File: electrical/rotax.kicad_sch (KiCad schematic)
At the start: 14 parts

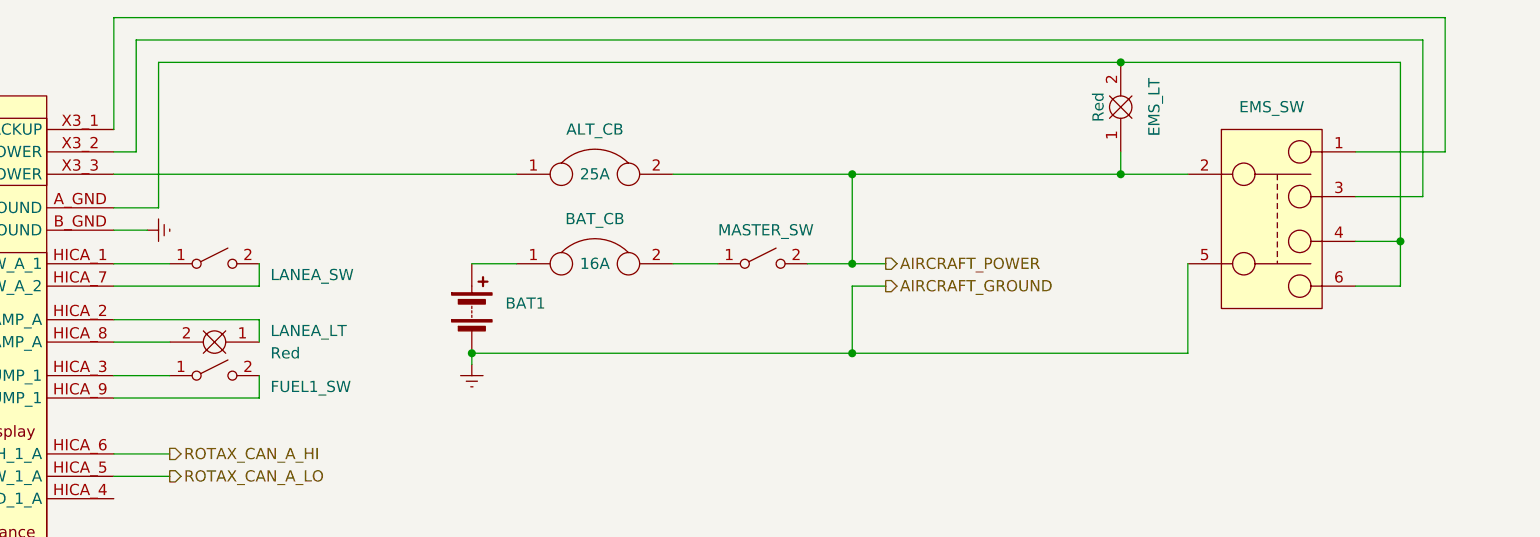
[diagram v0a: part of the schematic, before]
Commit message: Converted to breakers w/GAD 27 instead of VP-X.
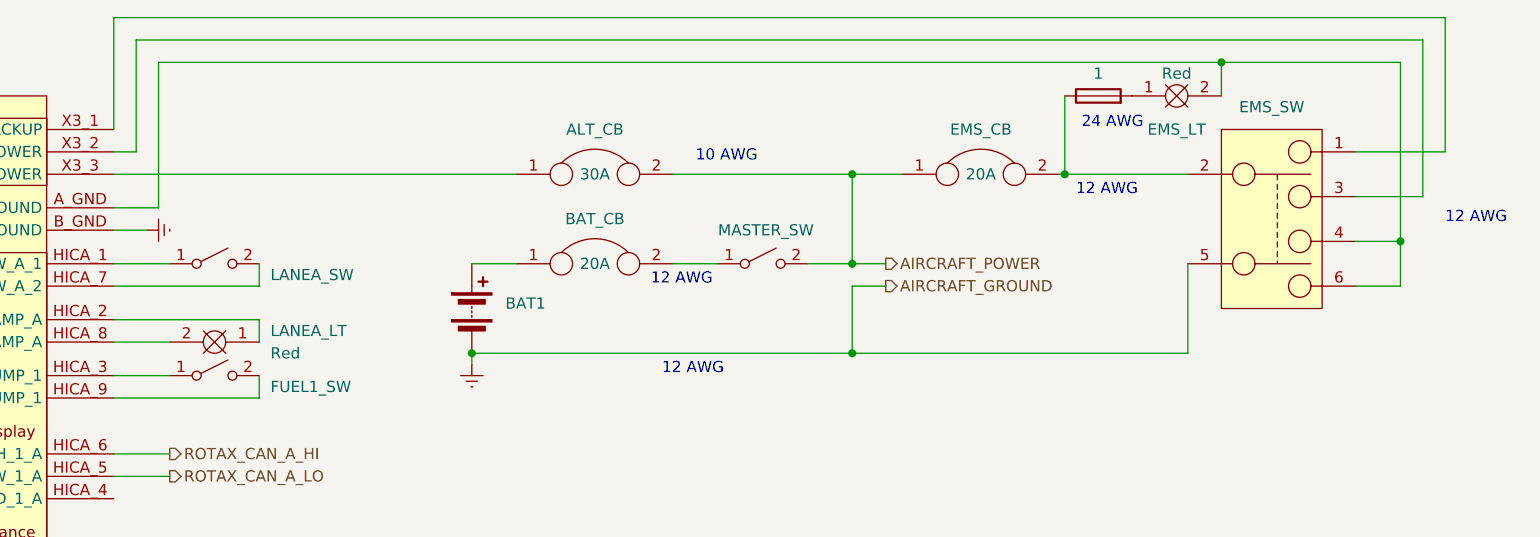
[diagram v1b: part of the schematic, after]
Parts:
- added EMS_CB: 20A, symbol flyerx:Circuit_Breaker
- added EMS_LT_FS: 1, symbol Device:Fuse
- ALT_CB: value 25A -> 30A
- BAT_CB: value 16A -> 20A
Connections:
- net AIRCRAFT_POWER: now also EMS_CB.1; no longer EMS_LT.1, EMS_SW.2
- new net: EMS_LT.1, EMS_LT_FS.2
- new net: EMS_CB.2, EMS_LT_FS.1, EMS_SW.2
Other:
- note added: "10 AWG"
- note added: "12 AWG"
- note added: "24 AWG"
- moved on the sheet: EMS_LT
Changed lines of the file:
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@@
     (title "Rotax Engine")
     (date "2024-02-13")
-    (rev "0.9.1")
+    (rev "1.0")
     (company "N915SN Angry Bird")
-  )
-  (junction (at 201.93 69.85) (diameter 0) (color 0 0 0 0)
+    (comment 1 "w/Breakers")
   )
   (junction (at 233.68 77.47) (diameter 0) (color 0 0 0 0)
   )
+  (junction (at 213.36 57.15) (diameter 0) (color 0 0 0 0)
+  )
   (junction (at 128.27 90.17) (diameter 0) (color 0 0 0 0)
   )
+  (junction (at 195.58 69.85) (diameter 0) (color 0 0 0 0)
+  )
   (junction (at 171.45 90.17) (diameter 0) (color 0 0 0 0)
   )
@@
   (junction (at 171.45 80.01) (diameter 0) (color 0 0 0 0)
   )
-  (junction (at 201.93 57.15) (diameter 0) (color 0 0 0 0)
-  )
   (wire (pts (xy 92.71 73.66) (xy 92.71 57.15))
     (stroke (width 0) (type default))
@@
     (stroke (width 0) (type default))
   )
-  (wire (pts (xy 201.93 69.85) (xy 209.55 69.85))
-    (stroke (width 0) (type default))
-  )
   (wire (pts (xy 171.45 90.17) (xy 209.55 90.17))
     (stroke (width 0) (type default))
@@
     (stroke (width 0) (type default))
   )
-  (wire (pts (xy 201.93 57.15) (xy 233.68 57.15))
+  (wire (pts (xy 195.58 60.96) (xy 195.58 69.85))
+    (stroke (width 0) (type default))
+  )
+  (wire (pts (xy 92.71 57.15) (xy 213.36 57.15))
     (stroke (width 0) (type default))
   )
@@
     (stroke (width 0) (type default))
   )
+  (wire (pts (xy 213.36 57.15) (xy 233.68 57.15))
+    (stroke (width 0) (type default))
+  )
   (wire (pts (xy 110.49 135.89) (xy 110.49 138.43))
     (stroke (width 0) (type default))
@@
     (stroke (width 0) (type default))
   )
+  (wire (pts (xy 194.945 69.85) (xy 195.58 69.85))
+    (stroke (width 0) (type default))
+  )
   (wire (pts (xy 104.14 92.71) (xy 104.14 95.25))
     (stroke (width 0) (type default))
@@
     (stroke (width 0) (type default))
   )
-  (wire (pts (xy 201.93 69.85) (xy 201.93 67.31))
-    (stroke (width 0) (type default))
-  )
   (wire (pts (xy 91.44 76.2) (xy 87.63 76.2))
     (stroke (width 0) (type default))
@@
     (stroke (width 0) (type default))
   )
-  (wire (pts (xy 171.45 69.85) (xy 201.93 69.85))
-    (stroke (width 0) (type default))
-  )
   (wire (pts (xy 171.45 80.01) (xy 171.45 69.85))
     (stroke (width 0) (type default))
@@
     (stroke (width 0) (type default))
   )
+  (wire (pts (xy 195.58 69.85) (xy 209.55 69.85))
+    (stroke (width 0) (type default))
+  )
   (wire (pts (xy 228.6 77.47) (xy 233.68 77.47))
     (stroke (width 0) (type default))
@@
     (stroke (width 0) (type default))
   )
+  (wire (pts (xy 213.36 57.15) (xy 213.36 60.96))
+    (stroke (width 0) (type default))
+  )
   (wire (pts (xy 151.13 80.01) (xy 156.21 80.01))
     (stroke (width 0) (type default))
   )
+  (wire (pts (xy 171.45 69.85) (xy 177.165 69.85))
+    (stroke (width 0) (type default))
+  )
   (wire (pts (xy 128.27 80.01) (xy 133.35 80.01))
     (stroke (width 0) (type default))
@@
     (stroke (width 0) (type default))
   )
-  (wire (pts (xy 92.71 57.15) (xy 201.93 57.15))
-    (stroke (width 0) (type default))
-  )
   (wire (pts (xy 87.63 129.54) (xy 110.49 129.54))
     (stroke (width 0) (type default))
@@
   (wire (pts (xy 110.49 125.73) (xy 87.63 125.73))
     (stroke (width 0) (type default))
+  )
+  (text "24 AWG" (at 197.485 64.77 0)
+    (effects (font (size 1.27 1.27)) (justify left bottom))
+  )
+  (text "12 AWG" (at 148.59 82.55 0)
+    (effects (font (size 1.27 1.27)) (justify left bottom))
+  )
+  (text "12 AWG" (at 238.76 75.565 0)
+    (effects (font (size 1.27 1.27)) (justify left bottom))
+  )
+  (text "12 AWG" (at 149.86 92.71 0)
+    (effects (font (size 1.27 1.27)) (justify left bottom))
+  )
+  (text "10 AWG" (at 153.67 68.58 0)
+    (effects (font (size 1.27 1.27)) (justify left bottom))
+  )
+  (text "12 AWG" (at 196.85 72.39 0)
+    (effects (font (size 1.27 1.27)) (justify left bottom))
   )
   (hierarchical_label "ROTAX_CAN_B_LO" (shape output) (at 95.25 153.67 0) (fields_autoplaced)
@@
       (effects (font (size 1.27 1.27)))
     )
-    (property "Value" "25A" (at 142.24 69.85 0)
+    (property "Value" "30A" (at 142.24 69.85 0)
       (effects (font (size 1.27 1.27)))
     )
@@
     )
   )
-  (symbol (lib_id "flyerx:Bulb") (at 203.2 63.5 270) (mirror x) (unit 1)
-    (in_bom yes) (on_board yes) (dnp no)
-    (property "Reference" "EMS_LT" (at 205.74 62.23 0)
-      (effects (font (size 1.27 1.27)))
-    )
-    (property "Value" "Red" (at 199.39 62.23 0)
-      (effects (font (size 1.27 1.27)))
-    )
-    (property "Footprint" "" (at 204.47 62.23 0)
-      (effects (font (size 1.27 1.27)) hide)
-    )
-    (property "Datasheet" "" (at 204.47 62.23 0)
+  (symbol (lib_id "flyerx:Bulb") (at 207.01 62.23 0) (mirror x) (unit 1)
+    (in_bom yes) (on_board yes) (dnp no)
+    (property "Reference" "EMS_LT" (at 208.28 64.77 0)
+      (effects (font (size 1.27 1.27)))
+    )
+    (property "Value" "Red" (at 208.28 58.42 0)
+      (effects (font (size 1.27 1.27)))
+    )
+    (property "Footprint" "" (at 208.28 63.5 0)
+      (effects (font (size 1.27 1.27)) hide)
+    )
+    (property "Datasheet" "" (at 208.28 63.5 0)
       (effects (font (size 1.27 1.27)) hide)
     )
@@
       (effects (font (size 1.27 1.27)))
     )
-    (property "Value" "16A" (at 142.24 80.01 0)
+    (property "Value" "20A" (at 142.24 80.01 0)
       (effects (font (size 1.27 1.27)))
     )
@@
         (path "/e8ec215a-dbe2-4eba-a577-e50a0a128049/2dfb13c9-19ab-4b61-8910-6455da71626b"
           (reference "START_SW") (unit 1)
+        )
+      )
+    )
+  )
+  (symbol (lib_id "flyerx:Circuit_Breaker") (at 186.055 67.31 0) (unit 1)
+    (in_bom yes) (on_board yes) (dnp no)
+    (property "Reference" "EMS_CB" (at 186.055 64.77 0)
+      (effects (font (size 1.27 1.27)))
+    )
+    (property "Value" "20A" (at 186.055 69.85 0)
+      (effects (font (size 1.27 1.27)))
+    )
+    (property "Footprint" "" (at 186.055 67.31 0)
+      (effects (font (size 1.27 1.27)) hide)
+    )
+    (property "Datasheet" "" (at 186.055 67.31 0)
+      (effects (font (size 1.27 1.27)) hide)
+    )
+    (pin "2")
+    (pin "1")
+    (instances
+      (project "electrical"
+        (path "/e8ec215a-dbe2-4eba-a577-e50a0a128049/2dfb13c9-19ab-4b61-8910-6455da71626b"
+          (reference "EMS_CB") (unit 1)
         )
       )
@@
         )
       )
+    )
+  )
+  (symbol (lib_id "Device:Fuse") (at 199.39 60.96 90) (unit 1)
+    (in_bom yes) (on_board yes) (dnp no)
+    (property "Reference" "EMS_LT_FS" (at 199.39 57.15 90)
+      (effects (font (size 1.27 1.27)) hide)
+    )
+    (property "Value" "1" (at 199.39 58.42 90)
+      (effects (font (size 1.27 1.27)))
+    )
+    (property "Footprint" "" (at 199.39 62.738 90)
+      (effects (font (size 1.27 1.27)) hide)
+    )
+    (property "Datasheet" "~" (at 199.39 60.96 0)
+      (effects (font (size 1.27 1.27)) hide)
+    )
+    (pin "1")
+    (pin "2")
+    (instances
+      (project "electrical"
+        (path "/e8ec215a-dbe2-4eba-a577-e50a0a128049/2dfb13c9-19ab-4b61-8910-6455da71626b"
+          (reference "EMS_LT_FS") (unit 1)
+        )
+      )

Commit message: Interim check-in. Not sure what I was doing.
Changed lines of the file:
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@@
+    (effects (font (size 1.27 1.27)) (justify left))
+  )
+  (hierarchical_label "MASTER_ON" (shape output) (at 178.435 100.33 0) (fields_autoplaced)
     (effects (font (size 1.27 1.27)) (justify left))
   )

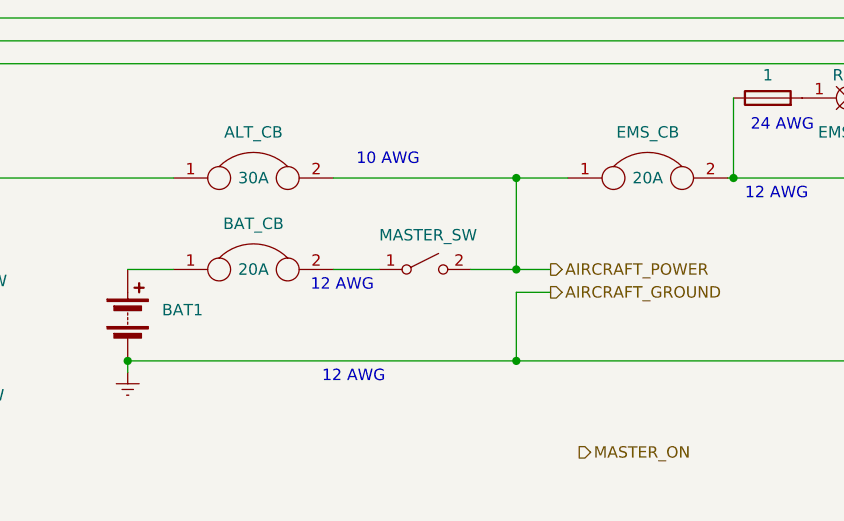
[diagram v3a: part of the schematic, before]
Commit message: Cleaned up power and smoke.
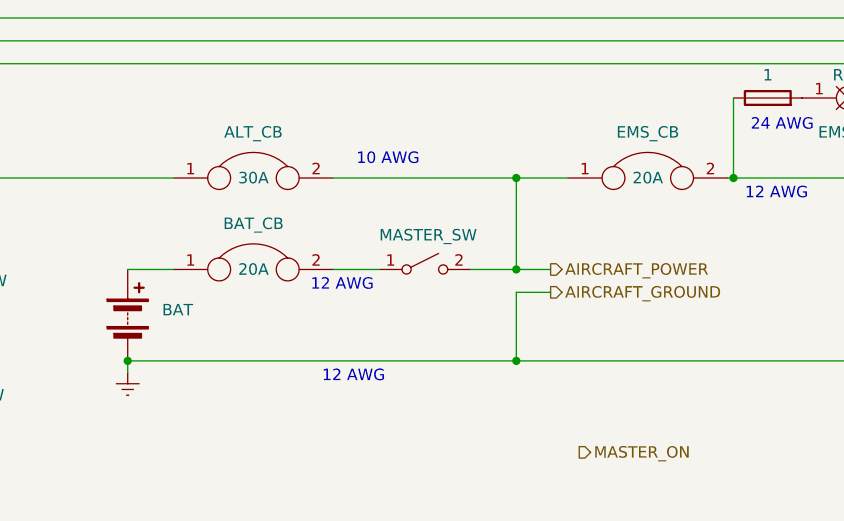
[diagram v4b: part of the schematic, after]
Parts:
- renumbered BAT1 to BAT
